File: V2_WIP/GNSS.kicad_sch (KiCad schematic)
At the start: 17 parts, among them J301 *USB_B_Micro, U301 USBLC6-2SC6, U401 *NEO-M9N

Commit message: updated list of changes in README.md
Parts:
- removed R301: 0R, Resistor_SMD:R_0603_1608Metric_Pad0.98x0.95mm_HandSolder, symbol Device:R_Small
- added C302: 1uF, Capacitor_SMD:C_0603_1608Metric_Pad1.08x0.95mm_HandSolder, symbol Device:C
- added Q5: BSS138, Package_TO_SOT_SMD:SOT-23, symbol Transistor_FET:BSS138
- added R402: 10, Resistor_SMD:R_0603_1608Metric_Pad0.98x0.95mm_HandSolder, symbol Device:R
- added R403, R404: 5k, Resistor_SMD:R_0603_1608Metric_Pad0.98x0.95mm_HandSolder, symbol Device:R
- added R405, R406: 27, Resistor_SMD:R_0603_1608Metric_Pad0.98x0.95mm_HandSolder, symbol Device:R
- added R407: 0R, Resistor_SMD:R_0603_1608Metric_Pad0.98x0.95mm_HandSolder, symbol Device:R
- added TP5: EXTINT, TestPoint:TestPoint_Pad_D1.0mm, symbol Connector:TestPoint
- AE301: value Antenna_Shield -> MCRF
- AE401: value Antenna_Shield -> SMA
- J301: footprint Connector_USB:USB_Micro-B_Wuerth_629105150521_CircularHoles -> KiCad:629105150521
- TP301, TP401, TP402: footprint TestPoint:TestPoint_Pad_D1.5mm -> TestPoint:TestPoint_Pad_D1.0mm
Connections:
- net +3V3: now also Q5.2 (S)
- net GND: now also C302.2, R403.1, R404.1, R407.1
- net RF: now reaches AE301.1 (A), AE401.1 (A), L401.1, U401.11 (RF_IN)
- net at U301.4 (I/O2): now also R406.1; no longer U401.5 (USB_DM)
- net V_USB: now reaches D301.2 (A), J301.1 (VBUS), U301.5 (VBUS)
- net V_USB: now also R402.2, R403.2
- net at U301.6 (I/O1): now also R405.2; no longer U401.6 (USB_DP)
- net VDD_USB: now reaches U401.7 (VDD_USB)
- net VDD_USB: now also C302.1, Q5.3 (D), R404.2
- net at U401.4 (EXTINT): now also TP5.1
- net at U401.8 (~{RESET}): now also R407.2
- new net: Q5.1 (G), R402.1
- new net DM: R406.2, U401.5 (USB_DM)
- new net DP: R405.1, U401.6 (USB_DP)
- no-connect marks 7 -> 5
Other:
- moved on the sheet: AE301, C401, C402, D301, J301, TP301, U301

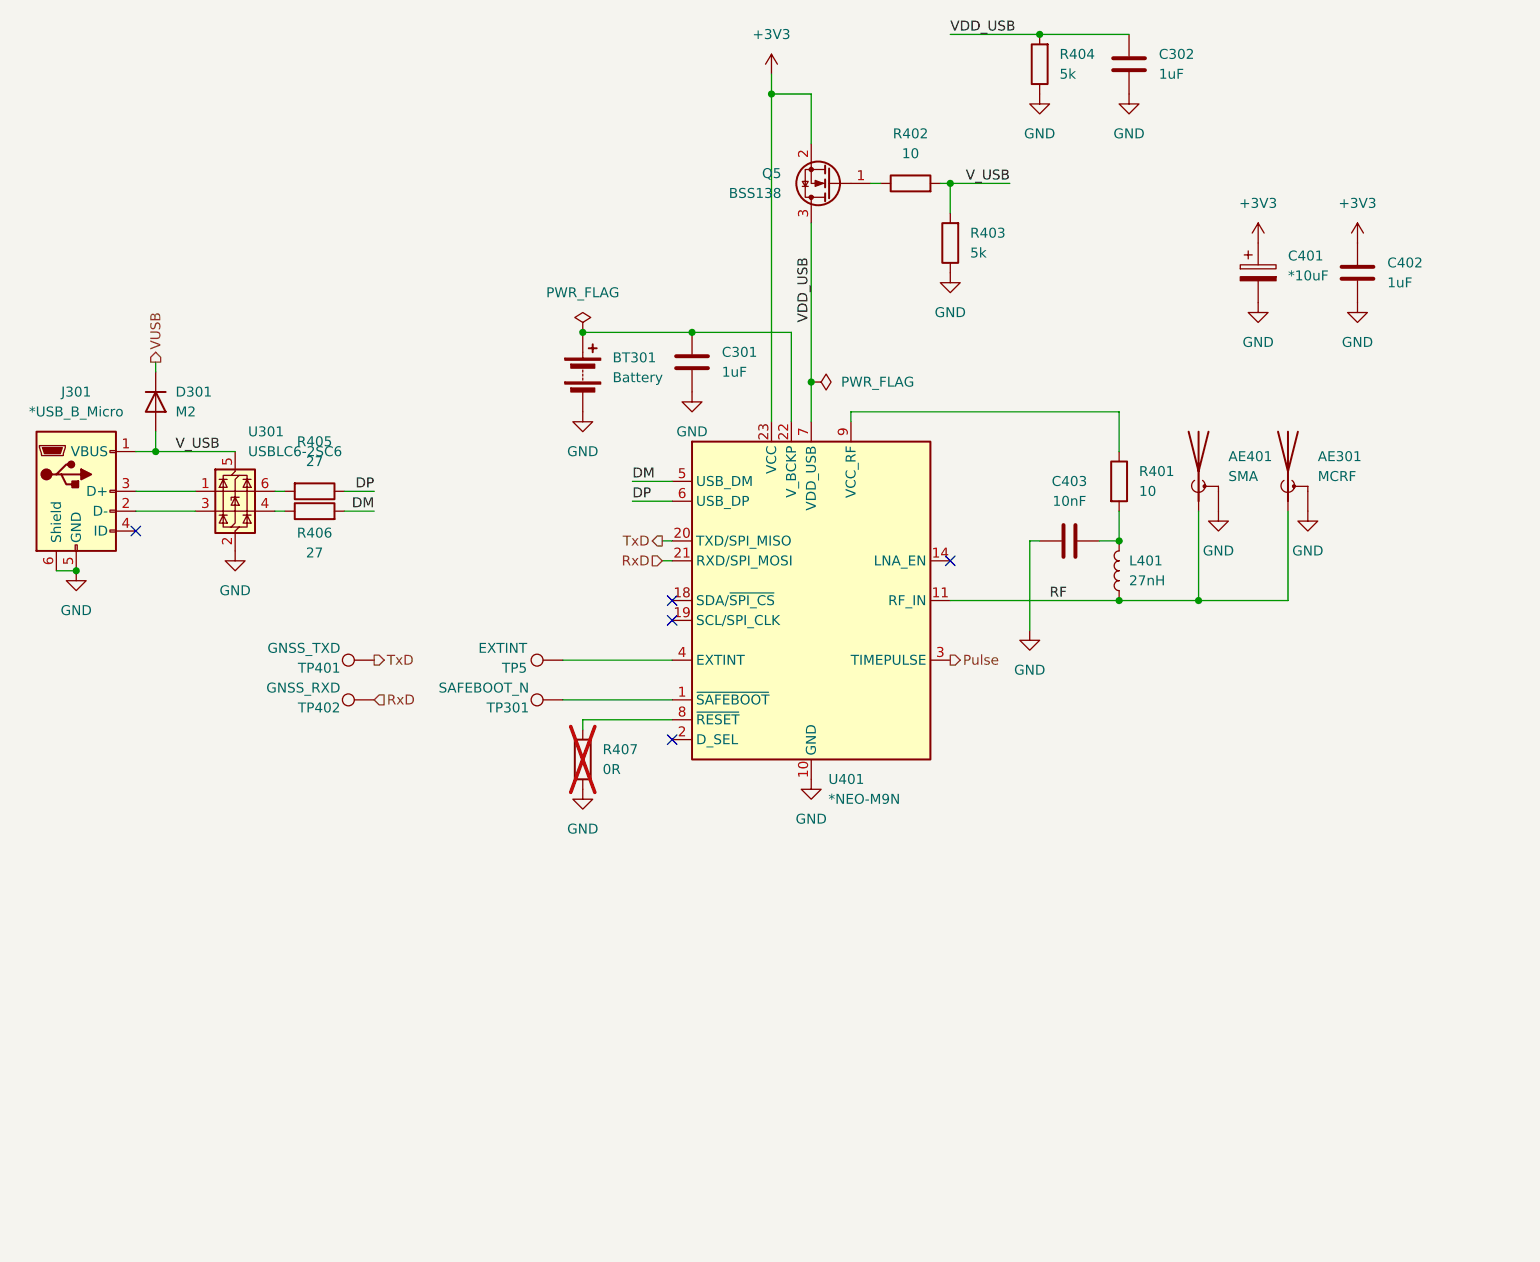
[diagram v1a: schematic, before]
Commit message: reworked the schematic, changed differential pairs and RF traces, small PCB adjustments
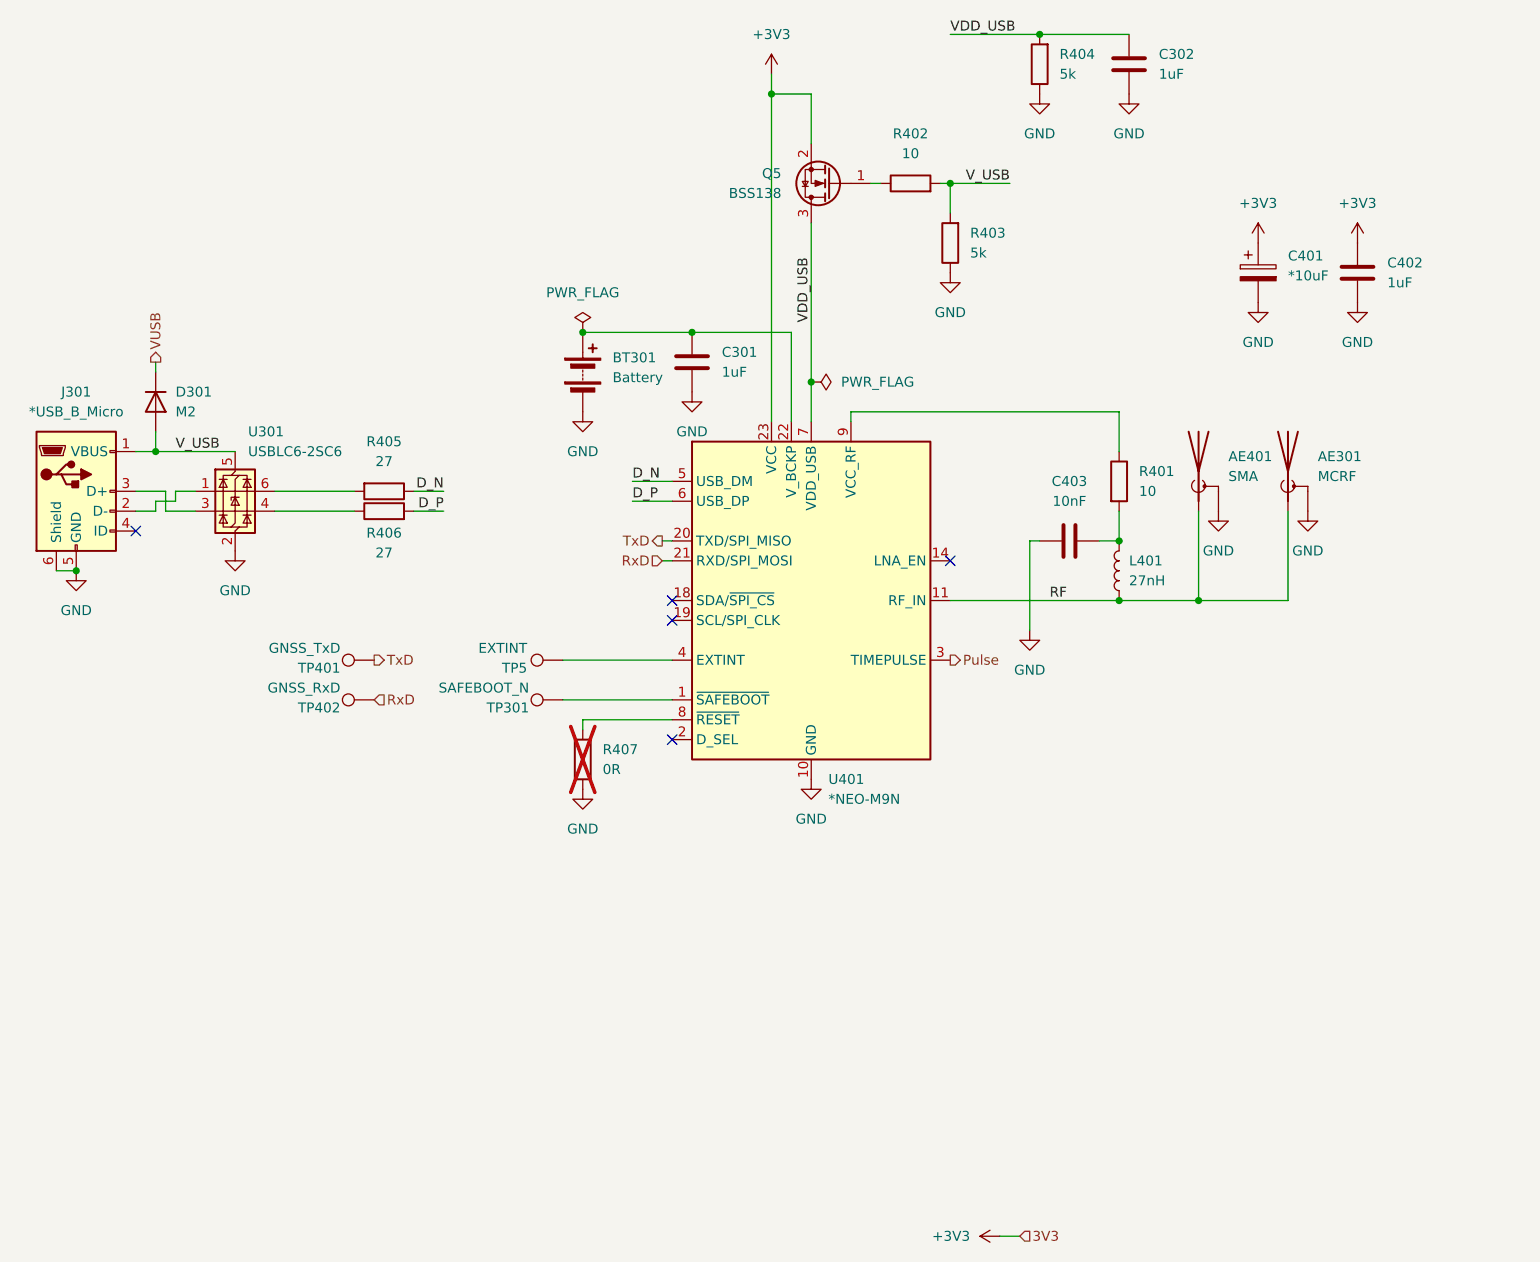
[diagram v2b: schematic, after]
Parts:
- C401: footprint Capacitor_Tantalum_SMD:CP_EIA-3528-15_AVX-H_Pad1.50x2.35mm_HandSolder -> Capacitor_Tantalum_SMD:CP_EIA-3528-21_Kemet-B_HandSolder
- TP401: value GNSS_TXD -> GNSS_TxD
- TP402: value GNSS_RXD -> GNSS_RxD
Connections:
- net at U301.1 (I/O1): now also J301.2 (D-); no longer J301.3 (D+)
- net at U301.3 (I/O2): now also J301.3 (D+); no longer J301.2 (D-)
- net DM renamed D_N
- net D_N: now also R405.1; no longer R406.2
- net DP renamed D_P
- net D_P: now also R406.2; no longer R405.1
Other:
- moved on the sheet: R405, R406

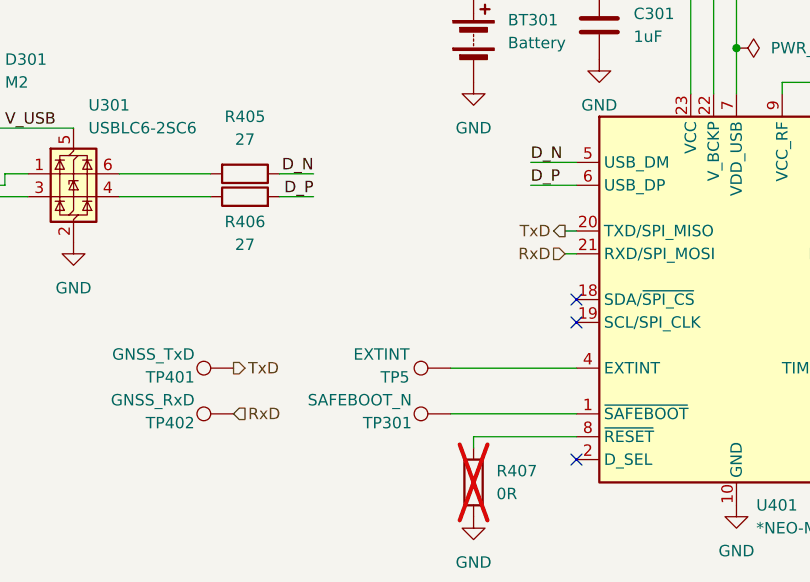
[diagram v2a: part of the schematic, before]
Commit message: switched Tx and Rx on GNSS module, added option to switch them, minor pcb changes
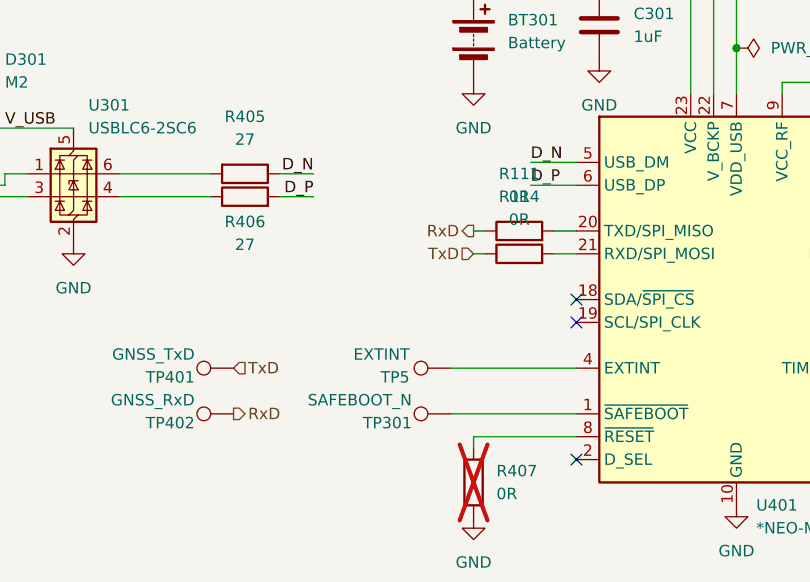
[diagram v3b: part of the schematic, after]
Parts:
- added R111, R114: 0R, Resistor_SMD:R_0603_1608Metric_Pad0.98x0.95mm_HandSolder, symbol Device:R
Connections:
- net RxD: now also R111.1; no longer U401.21 (RXD/SPI_MOSI)
- net TxD: now also R114.1; no longer U401.20 (TXD/SPI_MISO)
- new net: R114.2, U401.21 (RXD/SPI_MOSI)
- new net: R111.2, U401.20 (TXD/SPI_MISO)
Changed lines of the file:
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@@
 	(wire
 		(pts
-			(xy 120.65 102.87) (xy 121.92 102.87)
+			(xy 110.49 102.87) (xy 111.76 102.87)
 		)
 		(stroke
@@
 	(wire
 		(pts
-			(xy 120.65 100.33) (xy 121.92 100.33)
-		)
-		(stroke
-			(width 0)
-			(type default)
-		)
-	)
-	(wire
-		(pts
 			(xy 157.48 58.42) (xy 157.48 54.61)
 		)
@@
 	(wire
 		(pts
+			(xy 119.38 102.87) (xy 121.92 102.87)
+		)
+		(stroke
+			(width 0)
+			(type default)
+		)
+	)
+	(wire
+		(pts
 			(xy 139.7 43.18) (xy 139.7 49.53)
 		)
@@
 	(wire
 		(pts
+			(xy 119.38 100.33) (xy 121.92 100.33)
+		)
+		(stroke
+			(width 0)
+			(type default)
+		)
+	)
+	(wire
+		(pts
 			(xy 139.7 59.69) (xy 139.7 80.01)
+		)
+		(stroke
+			(width 0)
+			(type default)
+		)
+	)
+	(wire
+		(pts
+			(xy 110.49 100.33) (xy 111.76 100.33)
 		)
 		(stroke
@@
 	)
 	(hierarchical_label "RxD"
+		(shape output)
+		(at 110.49 100.33 180)
+		(effects
+			(font
+				(size 1.27 1.27)
+			)
+			(justify right)
+		)
+	)
+	(hierarchical_label "RxD"
+		(shape output)
+		(at 83.82 120.65 0)
+		(effects
+			(font
+				(size 1.27 1.27)
+			)
+			(justify left)
+		)
+	)
+	(hierarchical_label "TxD"
 		(shape input)
-		(at 120.65 102.87 180)
-		(effects
-			(font
-				(size 1.27 1.27)
-			)
-			(justify right)
-		)
-	)
-	(hierarchical_label "RxD"
-		(shape input)
-		(at 83.82 120.65 0)
-		(effects
-			(font
-				(size 1.27 1.27)
-			)
-			(justify left)
-		)
-	)
-	(hierarchical_label "TxD"
-		(shape output)
 		(at 83.82 115.57 0)
 		(effects
@@
 		)
 	)
+	(hierarchical_label "TxD"
+		(shape input)
+		(at 110.49 102.87 180)
+		(effects
+			(font
+				(size 1.27 1.27)
+			)
+			(justify right)
+		)
+	)
 	(hierarchical_label "Pulse"
 		(shape output)
@@
 			)
 			(justify left)
-		)
-	)
-	(hierarchical_label "TxD"
-		(shape output)
-		(at 120.65 100.33 180)
-		(effects
-			(font
-				(size 1.27 1.27)
-			)
-			(justify right)
 		)
 	)
@@
 	)
 	(symbol
+		(lib_id "Device:R")
+		(at 115.57 102.87 90)
+		(unit 1)
+		(body_style 1)
+		(exclude_from_sim no)
+		(in_bom yes)
+		(on_board yes)
+		(in_pos_files yes)
+		(dnp no)
+		(fields_autoplaced yes)
+		(property "Reference" "R114"
+			(at 115.57 96.52 90)
+			(show_name no)
+			(do_not_autoplace no)
+			(effects
+				(font
+					(size 1.27 1.27)
+				)
+			)
+		)
+		(property "Value" "0R"
+			(at 115.57 99.06 90)
+			(show_name no)
+			(do_not_autoplace no)
+			(effects
+				(font
+					(size 1.27 1.27)
+				)
+			)
+		)
+		(property "Footprint" "Resistor_SMD:R_0603_1608Metric_Pad0.98x0.95mm_HandSolder"
+			(at 115.57 104.648 90)
+			(hide yes)
+			(show_name no)
+			(do_not_autoplace no)
+			(effects
+				(font
+					(size 1.27 1.27)
+				)
+			)
+		)
+		(property "Datasheet" "https://cz.mouser.com/ProductDetail/SEI-Stackpole/RNCE0603BTE2K00?qs=sGAEpiMZZMtlubZbdhIBIGfmJML7fLMVr3bVQ0UuJPQ%3D"
+			(at 115.57 102.87 0)
+			(hide yes)
+			(show_name no)
+			(do_not_autoplace no)
+			(effects
+				(font
+					(size 1.27 1.27)
+				)
+			)
+		)
+		(property "Description" "Resistor"
+			(at 115.57 102.87 0)
+			(hide yes)
+			(show_name no)
+			(do_not_autoplace no)
+			(effects
+				(font
+					(size 1.27 1.27)
+				)
+			)
+		)
+		(property "Purchase-URL" ""
+			(at 115.57 102.87 0)
+			(hide yes)
+			(show_name no)
+			(do_not_autoplace no)
+			(effects
+				(font
+					(size 1.27 1.27)
+				)
+			)
+		)
+		(pin "1"
+		)
+		(pin "2"
+		)
+		(instances
+			(project "gps"
+				(path "/00526ddc-5304-4072-af1e-192a9e7e83da/5cdf5b9a-bc05-4fbb-ac1a-8c1a969964f2"
+					(reference "R114")
+					(unit 1)
+				)
+			)
+		)
+	)
+	(symbol
 		(lib_id "power:+3V3")
 		(at 163.83 189.23 90)
@@
 					(unit 1)
 				)
+			)
+		)
+	)
+	(symbol
+		(lib_id "Device:R")
+		(at 115.57 100.33 90)
+		(unit 1)
+		(body_style 1)
+		(exclude_from_sim no)
+		(in_bom yes)
+		(on_board yes)
+		(in_pos_files yes)
+		(dnp no)
+		(fields_autoplaced yes)
+		(property "Reference" "R111"
+			(at 115.57 93.98 90)
+			(show_name no)
+			(do_not_autoplace no)
+			(effects
+				(font
+					(size 1.27 1.27)
+				)
+			)
+		)
+		(property "Value" "0R"
+			(at 115.57 96.52 90)
+			(show_name no)
+			(do_not_autoplace no)
+			(effects
+				(font
+					(size 1.27 1.27)
+				)
+			)
+		)
+		(property "Footprint" "Resistor_SMD:R_0603_1608Metric_Pad0.98x0.95mm_HandSolder"
+			(at 115.57 102.108 90)
+			(hide yes)
+			(show_name no)
+			(do_not_autoplace no)
+			(effects
+				(font
+					(size 1.27 1.27)
+				)
+			)
+		)
+		(property "Datasheet" "https://cz.mouser.com/ProductDetail/SEI-Stackpole/RNCE0603BTE2K00?qs=sGAEpiMZZMtlubZbdhIBIGfmJML7fLMVr3bVQ0UuJPQ%3D"
+			(at 115.57 100.33 0)
+			(hide yes)
+			(show_name no)
+			(do_not_autoplace no)
+			(effects
+				(font
+					(size 1.27 1.27)
+				)
+			)
+		)
+		(property "Description" "Resistor"
+			(at 115.57 100.33 0)
+			(hide yes)
+			(show_name no)
+			(do_not_autoplace no)
+			(effects
+				(font
+					(size 1.27 1.27)
+				)
+			)
+		)
+		(property "Purchase-URL" ""
+			(at 115.57 100.33 0)
+			(hide yes)
+			(show_name no)
+			(do_not_autoplace no)
+			(effects
+				(font
+					(size 1.27 1.27)
+				)
+			)
+		)
+		(pin "1"
+		)
+		(pin "2"
+		)
+		(instances
+			(project "gps"
+				(path "/00526ddc-5304-4072-af1e-192a9e7e83da/5cdf5b9a-bc05-4fbb-ac1a-8c1a969964f2"
+					(reference "R111")
+					(unit 1)
+				)
